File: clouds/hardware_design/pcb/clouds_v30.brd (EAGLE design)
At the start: 88.9 x 106 mm, 156 parts, among them IC1 74HC595D, IC10 TL072D, IC2 LM1117-3.3, IC3 MCP6002, IC4 MCP6004, IC5 STM32F405RGT6, IC6 LM4040B10, IC7 LM1117-3.3, IC8 WM8731, IC9 TL072D, J1 PJ301_THONKICONN6, J10 PJ301_THONKICONN6, J11 PJ301_THONKICONN6, J12 PJ301_THONKICONN6, J2 PJ301_THONKICONN6, J3 PJ301_THONKICONN6, J4 PJ301_THONKICONN6, J5 PJ301_THONKICONN6, J6 PJ301_THONKICONN6, J7 PJ301_THONKICONN6, J8 PJ301_THONKICONN6, J9 PJ301_THONKICONN6, Q1 MMBT3904, Q2 MMBT3904, Q3 8MHz, Q4 12.288MHz, SW1 LP4OA1PBCT

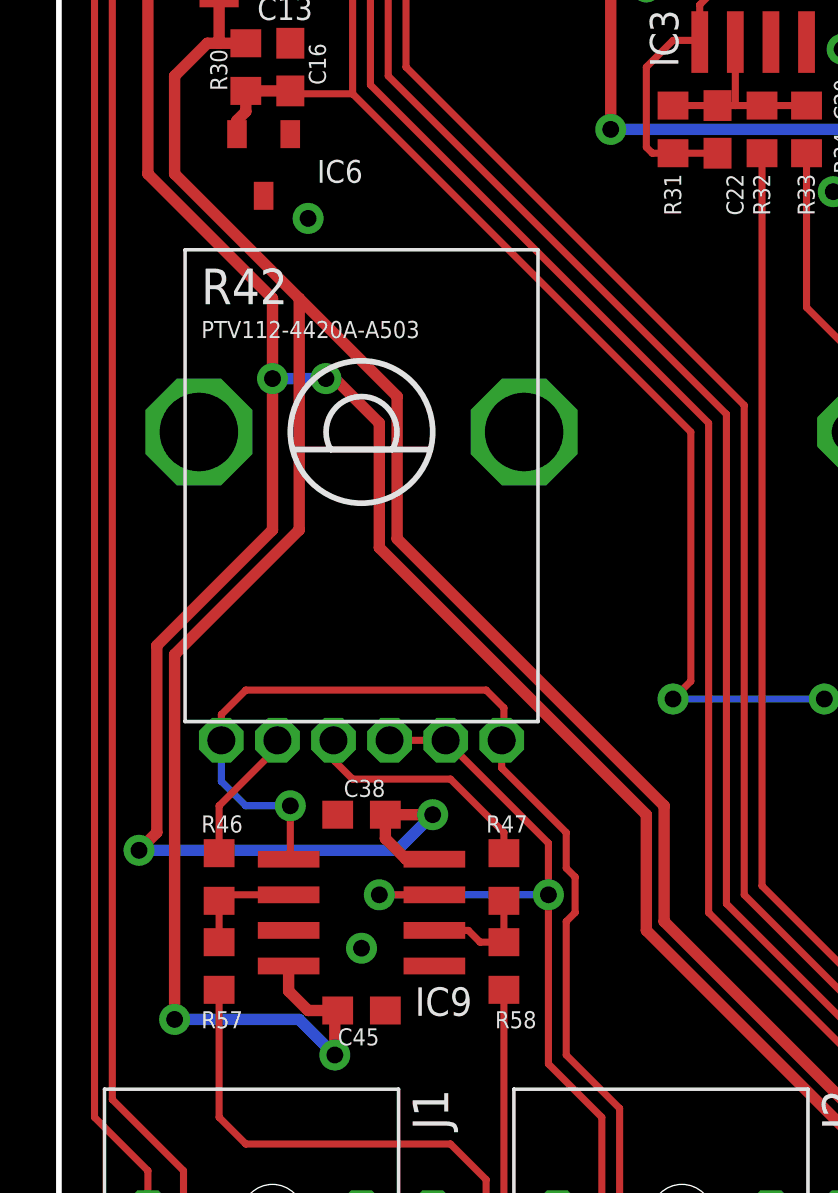
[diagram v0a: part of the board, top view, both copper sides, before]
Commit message: convert R42 from BOURNS_PTV112 to ALPHA_RD902F-040
Signed-off-by: vladimir <vladimir@pantelic.net>
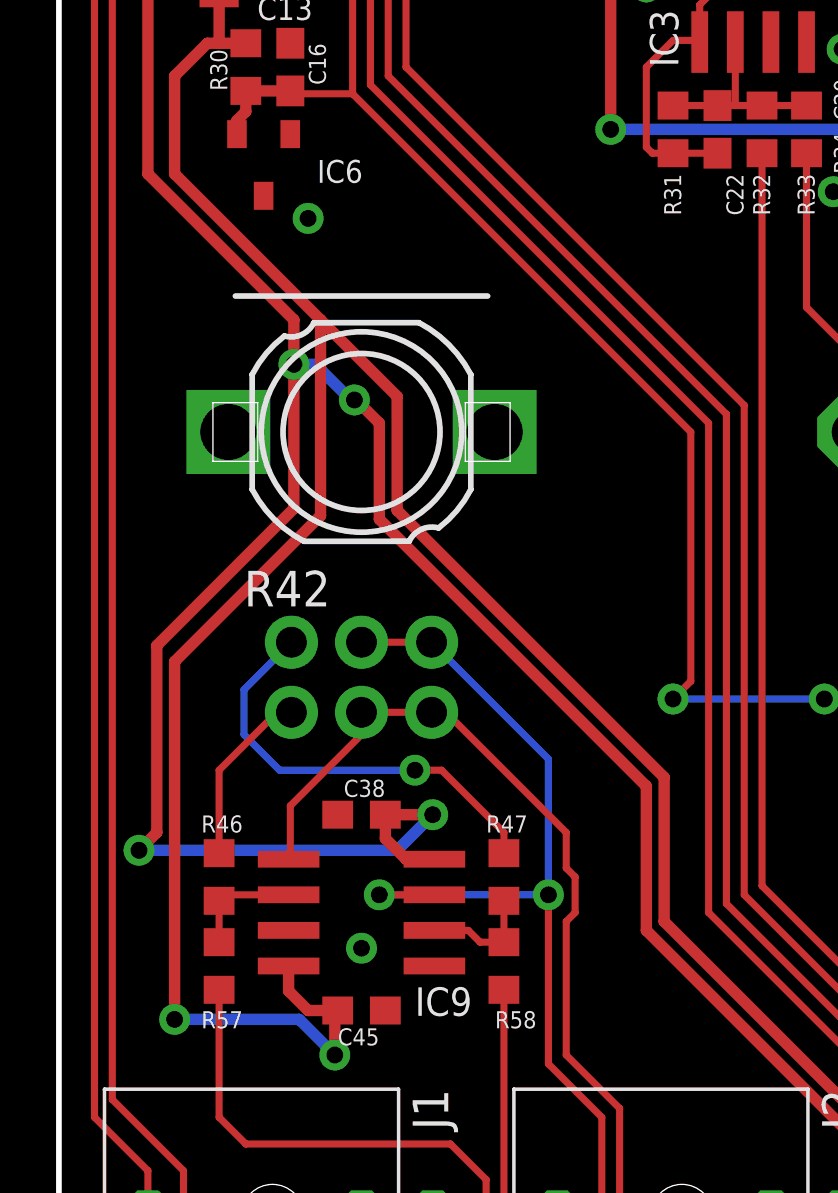
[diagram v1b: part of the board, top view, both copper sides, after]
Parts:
- R42: value PTV112-4420A-A503 -> 50kA; device og-pots:BOURNS_PTV112 -> 00vp:ALPHA_RD902F-040
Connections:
- net N$42: now also R42.1-2, R42.1-3; no longer R42.2P, R42.3P
- net N$51: now also R42.2-2, R42.2-3; no longer R42.2, R42.3
- net N$52: now also R42.1-1; no longer R42.1P
- net N$53: now also R42.2-1; no longer R42.1
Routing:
- net N$51: track 135.3 -> 127.5 mm, vias 3 -> 2
- net N$52: track 8.59 -> 15.5 mm, vias 0 -> 1
- net N$42: track 125.0 -> 129.2 mm
- net N$53: track 4.89 -> 6.42 mm
